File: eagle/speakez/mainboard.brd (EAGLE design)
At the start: 39 parts, among them U1 +12v

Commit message: tweaked some clearances
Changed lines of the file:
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@@
 <?xml version="1.0" encoding="utf-8"?>
 <!DOCTYPE eagle SYSTEM "eagle.dtd">
-<eagle version="7.7.0">
+<eagle version="7.6.0">
 <drawing>
 <settings>
@@
 <setting verticaltext="up"/>
 </settings>
-<grid distance="0.01" unitdist="inch" unit="inch" style="lines" multiple="1" display="yes" altdistance="0.025" altunitdist="inch" altunit="inch"/>
+<grid distance="0.01" unitdist="inch" unit="inch" style="lines" multiple="1" display="no" altdistance="0.025" altunitdist="inch" altunit="inch"/>
 <layers>
 <layer number="1" name="Top" color="4" fill="1" visible="yes" active="yes"/>
@@
 </class>
 </classes>
-<designrules name="default">
+<designrules name="default *">
 <description language="de">&lt;b&gt;EAGLE Design Rules&lt;/b&gt;
 &lt;p&gt;
@@
 <param name="mtCopper" value="0.035mm 0.035mm 0.035mm 0.035mm 0.035mm 0.035mm 0.035mm 0.035mm 0.035mm 0.035mm 0.035mm 0.035mm 0.035mm 0.035mm 0.035mm 0.035mm"/>
 <param name="mtIsolate" value="1.5mm 0.15mm 0.2mm 0.15mm 0.2mm 0.15mm 0.2mm 0.15mm 0.2mm 0.15mm 0.2mm 0.15mm 0.2mm 0.15mm 0.2mm"/>
-<param name="mdWireWire" value="8mil"/>
-<param name="mdWirePad" value="8mil"/>
-<param name="mdWireVia" value="8mil"/>
-<param name="mdPadPad" value="8mil"/>
-<param name="mdPadVia" value="8mil"/>
-<param name="mdViaVia" value="8mil"/>
-<param name="mdSmdPad" value="8mil"/>
-<param name="mdSmdVia" value="8mil"/>
-<param name="mdSmdSmd" value="8mil"/>
+<param name="mdWireWire" value="6mil"/>
+<param name="mdWirePad" value="6mil"/>
+<param name="mdWireVia" value="6mil"/>
+<param name="mdPadPad" value="6mil"/>
+<param name="mdPadVia" value="6mil"/>
+<param name="mdViaVia" value="6mil"/>
+<param name="mdSmdPad" value="6mil"/>
+<param name="mdSmdVia" value="6mil"/>
+<param name="mdSmdSmd" value="6mil"/>
 <param name="mdViaViaSameLayer" value="8mil"/>
 <param name="mnLayersViaInSmd" value="2"/>
-<param name="mdCopperDimension" value="40mil"/>
-<param name="mdDrill" value="8mil"/>
+<param name="mdCopperDimension" value="6mil"/>
+<param name="mdDrill" value="6mil"/>
 <param name="mdSmdStop" value="0mil"/>
-<param name="msWidth" value="10mil"/>
-<param name="msDrill" value="24mil"/>
+<param name="msWidth" value="6mil"/>
+<param name="msDrill" value="4mil"/>
 <param name="msMicroVia" value="9.99mm"/>
 <param name="msBlindViaRatio" value="0.5"/>
@@
 <wire x1="32.766" y1="31.242" x2="33.02" y2="30.988" width="0.254" layer="16"/>
 <wire x1="33.02" y1="30.988" x2="33.02" y2="29.21" width="0.254" layer="16"/>
-<wire x1="33.02" y1="29.21" x2="31.496" y2="27.686" width="0.254" layer="16"/>
-<wire x1="31.496" y1="27.686" x2="29.718" y2="27.686" width="0.254" layer="16"/>
+<wire x1="33.02" y1="29.21" x2="31.75" y2="27.94" width="0.254" layer="16"/>
+<wire x1="31.75" y1="27.94" x2="29.718" y2="27.686" width="0.254" layer="16"/>
 <wire x1="29.718" y1="27.686" x2="28.194" y2="29.21" width="0.254" layer="16"/>
 </signal>
@@
 <wire x1="11.176" y1="2.286" x2="12.33" y2="9.652" width="0" layer="19" extent="1-1"/>
 <wire x1="28.956" y1="2.286" x2="26.416" y2="2.286" width="0" layer="19" extent="1-1"/>
-<wire x1="31.496" y1="2.286" x2="28.956" y2="2.286" width="0" layer="19" extent="1-1"/>
 </signal>
 <signal name="DATA">
@@
 <wire x1="38.608" y1="33.782" x2="36.068" y2="31.242" width="0.254" layer="1"/>
 <wire x1="36.068" y1="31.242" x2="34.544" y2="31.242" width="0.254" layer="1"/>
-<wire x1="34.544" y1="31.242" x2="30.988" y2="27.686" width="0.254" layer="1"/>
-<wire x1="30.988" y1="27.686" x2="30.4038" y2="27.686" width="0.254" layer="1"/>
+<wire x1="34.544" y1="31.242" x2="31.496" y2="27.686" width="0.254" layer="1"/>
+<wire x1="31.496" y1="27.686" x2="30.4038" y2="27.686" width="0.254" layer="1"/>
 <wire x1="30.4038" y1="27.686" x2="30.353" y2="27.7368" width="0.254" layer="1"/>
 <wire x1="16.256" y1="4.826" x2="14.986" y2="3.048" width="0.254" layer="16"/>

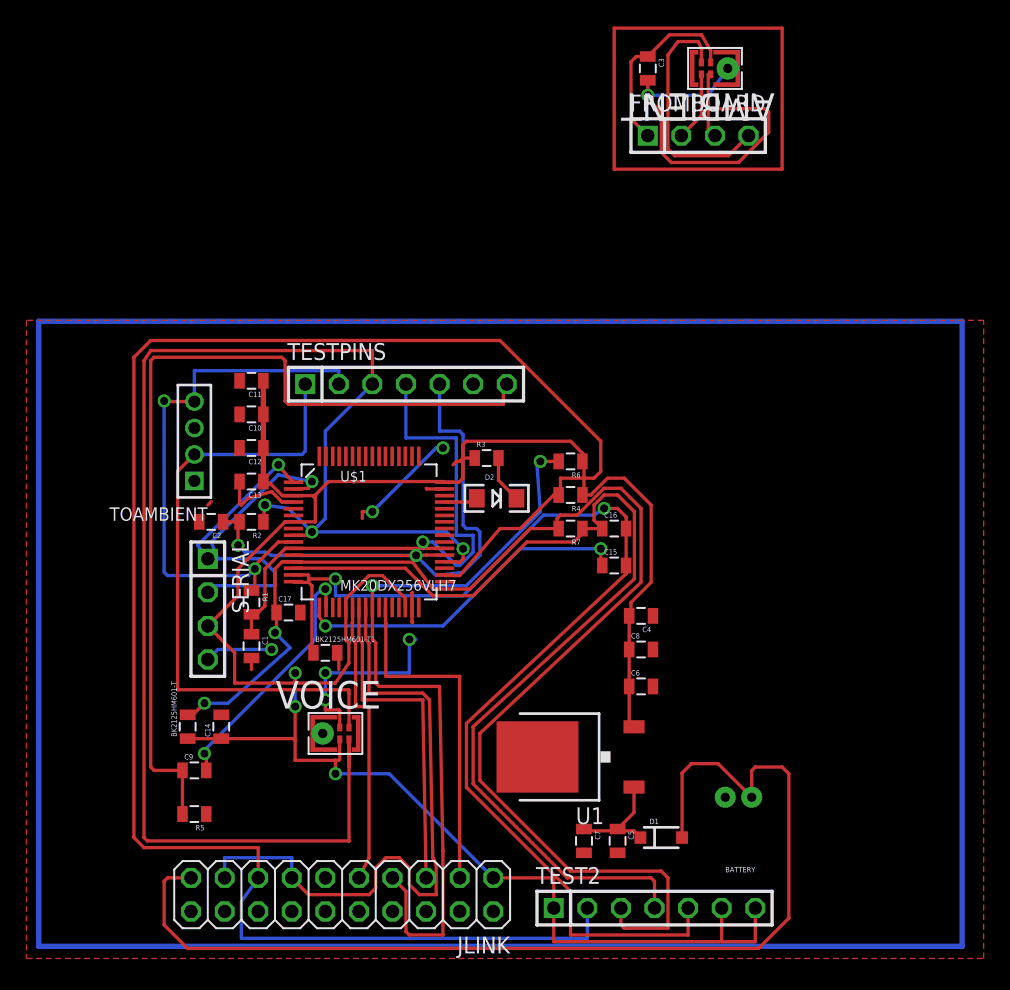
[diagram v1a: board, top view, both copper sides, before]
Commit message: fixed lots of clearance issues, added headers for filter testing
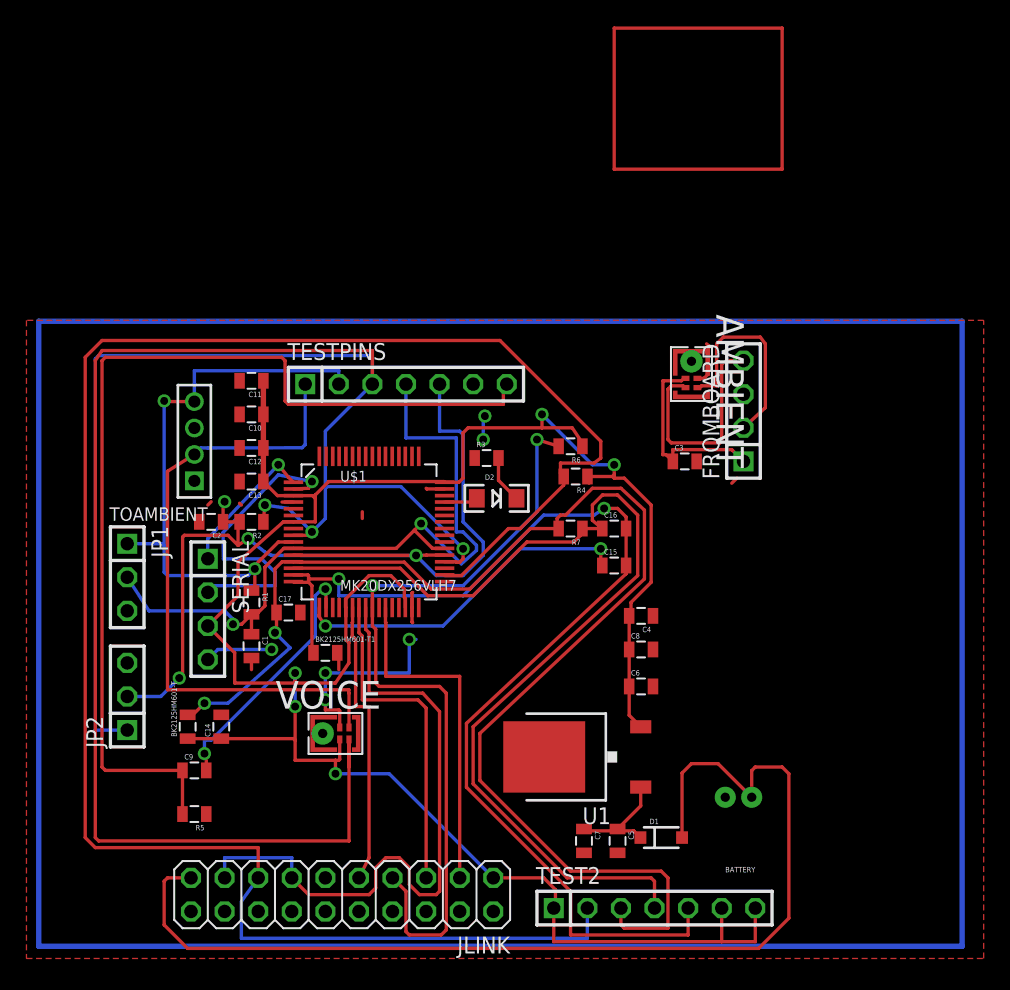
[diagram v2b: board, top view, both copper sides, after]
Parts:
- added JP1, JP2: (no value), pinhead:1X03
- moved C3 29.8 mm to (48.5, 36.3), turned to 0 degrees
- moved AMBIENT 23.2 mm to (49.0, 42.9), turned to 270 degrees
- moved FROMBOARD 21.1 mm to (53.0, 40.1), turned to 90 degrees
- moved R4 1.45 mm to (40.3, 35.2)
- moved R6 1.14 mm to (39.9, 37.5)
- moved U1 0.51 mm to (40.4, 14.0)
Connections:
- net DATA: now also JP2.1
- net GND: now also JP1.3, JP2.3
- net N$1: now also JP1.2
- net N$10: now also JP1.1
- net N$2: now also JP2.2
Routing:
- net DATA: track 116.3 -> 177.4 mm
- net GND: track 76.4 -> 33.2 mm, vias 7 -> 6
- net N$2: track 49.8 -> 71.5 mm, vias 2 -> 4
- net N$1: track 43.0 -> 56.6 mm, vias 1 -> 2
- net N$6: track 5.26 -> 15.9 mm
- net N$28: track 68.2 -> 75.6 mm
- net RESET: track 138.9 -> 146.2 mm
- net DECOUPLED: track 170.5 -> 177.6 mm, vias 3 -> 5
- net N$10: track 42.4 -> 45.3 mm
- net N$24: track 58.9 -> 60.8 mm
- net N$8: track 18.5 -> 17.2 mm
- net TEST-PINS: track 47.7 -> 48.7 mm
- net N$26: track 23.9 -> 23.0 mm
- net N$25: track 11.6 -> 11.0 mm

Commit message: resolved all conflicts. planning to add silkscreen next
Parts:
- moved C4 5.11 mm to (42.3, 20.4)
- moved C16 5.11 mm to (40.3, 27.1)
- moved R4 5.11 mm to (37.3, 31.0)
- moved R7 5.11 mm to (37.0, 27.1)
- moved C15 5.11 mm to (40.3, 24.3)
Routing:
- net N$12: track 46.7 -> 0.00 mm
- net N$11: track 234.2 -> 210.6 mm
- net N$30: track 101.8 -> 92.0 mm
- net N$20: track 87.6 -> 77.9 mm
- net N$22: track 77.6 -> 68.1 mm
- net N$31: track 26.1 -> 21.5 mm
- net DECOUPLED: track 177.6 -> 181.0 mm
- net RESET: track 146.2 -> 147.3 mm

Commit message: corrected battery and voltage regulator
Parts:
- removed D1: 1N5819HW-7-F, SparkFun-DiscreteSemi:SOD-123
- added D3: 1N5819HW-7-F, SparkFun-DiscreteSemi:SOD-123
- added TP1, TP10, TP11, TP2, TP3, TP4, TP5, TP6, TP7, TP8, TP9: TEST-POINT2, SparkFun-Passives:PAD.02X.02
- BATTERY: device SparkFun-Connectors:JST-2-PTH-NS -> pinhead:1X02
- U1: device SparkFun-PowerIC:TO-252 -> LP38691:TO-252
- moved U1 14.0 mm to (52.2, 21.5), turned to 0 degrees
- renumbered JP1 to AMB-FILT, JP2 to VOC-FILT
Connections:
- net N$6 renamed CLK2-A
- net N$7 renamed VDD-DECOUP-A
- net N$8 renamed DATA2-A
- removed net DECOUPLED: BK2125HM601-T.1, C10.1, C11.1, C12.1, C13.1, C14.1, C4.2, C6.1, C8.1, JLINK.1, R4.1, R6.1, SERIAL.3, TEST2.1, TEST2.6, TEST2.7, U$1.21, U$1.3, U$1.30, U$1.48, U$1.7, U1.2, VOICE.4
- removed net TEST-PINS: TESTPINS.1, TOAMBIENT.2, VOICE.1
- new net CLK: TESTPINS.1, TOAMBIENT.2, U$1.51, VOICE.1
- new net DATA2: AMB-FILT.1, R1.1, TESTPINS.2, TOAMBIENT.4, U$1.10, U$1.35
- new net N$12: TP9.P$1, U$1.60
- new net N$18: TP10.P$1, U$1.61
- new net N$21: TP11.P$1, U$1.62
- new net N$3: TP7.P$1, U$1.52
- new net N$4: TP6.P$1, U$1.53
- new net N$5: TP1.P$1, U$1.54
- new net N$6: TP2.P$1, U$1.55
- new net N$7: TP3.P$1, U$1.56
- new net N$8: TP4.P$1, U$1.57
- new net VDD-DECOUP: BK2125HM601-T.1, C10.1, C11.1, C12.1, C13.1, C14.1, C4.2, C6.1, C8.1, JLINK.1, R4.1, R6.1, SERIAL.3, TEST2.1, TEST2.6, TEST2.7, TOAMBIENT.1, U$1.21, U$1.3, U$1.30, U$1.48, U$1.7, U1.1, VOICE.4
- net +5V: now also D3.A; no longer D1.A
- net N$10: now also TP8.P$1, U$1.59; no longer AMB-FILT.1, R1.1, TESTPINS.2, TOAMBIENT.4, U$1.10
- net N$15: now also D3.C, U1.2; no longer D1.C, U1.1
- net N$9: now also TP5.P$1, U$1.58; no longer TOAMBIENT.1
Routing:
- net VDD-DECOUP: track 0.00 -> 183.7 mm, vias 0 -> 5
- net DECOUPLED: track 181.0 -> 0.00 mm, vias 5 -> 0
- net CLK: track 0.00 -> 60.7 mm
- net TEST-PINS: track 48.7 -> 0.00 mm
- net DATA2: track 0.00 -> 45.3 mm, vias 0 -> 2
- net N$10: track 45.3 -> 3.35 mm, vias 2 -> 0
- net N$15: track 8.74 -> 19.0 mm
- net +5V: track 81.9 -> 77.0 mm
- net GND: track 33.2 -> 37.4 mm, vias 6 -> 7
- net N$12: track 0.00 -> 3.40 mm
- net N$9: track 0.00 -> 3.29 mm
- net N$8: track 0.00 -> 3.24 mm
- net N$7: track 0.00 -> 3.18 mm
- net N$6: track 0.00 -> 3.13 mm
- net N$5: track 0.00 -> 3.07 mm
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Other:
- board text added: "CLK"
- board text added: "DATA"
- board text added: "GND"
- board text added: "IN"
- board text added: "OUT"
- board text added: "VDD"

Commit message: board all routed + silkcreening!!! :grin:
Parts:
- moved TP10 0.64 mm to (20.4, 39.6)
- moved TP11 0.64 mm to (21.1, 39.6)
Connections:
- net N$18: now also U$1.64; no longer U$1.61
- net N$21: now also U$1.63; no longer U$1.62
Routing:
- net DATA2: track 45.3 -> 80.4 mm, vias 2 -> 4
- net GND: track 37.4 -> 50.4 mm, vias 7 -> 11
- net VDD-DECOUP: track 183.7 -> 192.7 mm
- net DATA: track 177.8 -> 173.6 mm
- net N$18: track 0.00 -> 3.10 mm
- net N$21: track 0.00 -> 3.05 mm
- net CLK: track 60.7 -> 63.3 mm, vias 0 -> 1
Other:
- board text added: "+"
- board text added: "DAC"
- board text added: "DATA A"
- board text added: "DATA V"
- board text added: "DATA-V"
- board text added: "FILT A"
- board text added: "FILT V"
- board text added: "RX"
- board text added: "SpeakEZ 2.009 Orange Rev 1.0 #OJ"
- board text added: "TX"
- board text added: "rev 1.0 #OJ"
